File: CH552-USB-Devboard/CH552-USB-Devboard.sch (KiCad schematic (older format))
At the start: 38 parts, among them J1 Conn_01x11_Male, J2 Conn_01x11_Male, J3 USB_C_Receptacle, J4 USB_C_Receptacle, SW1 SW_Push, SW2 SW_Push, U1 CH552T, U2 CH552G

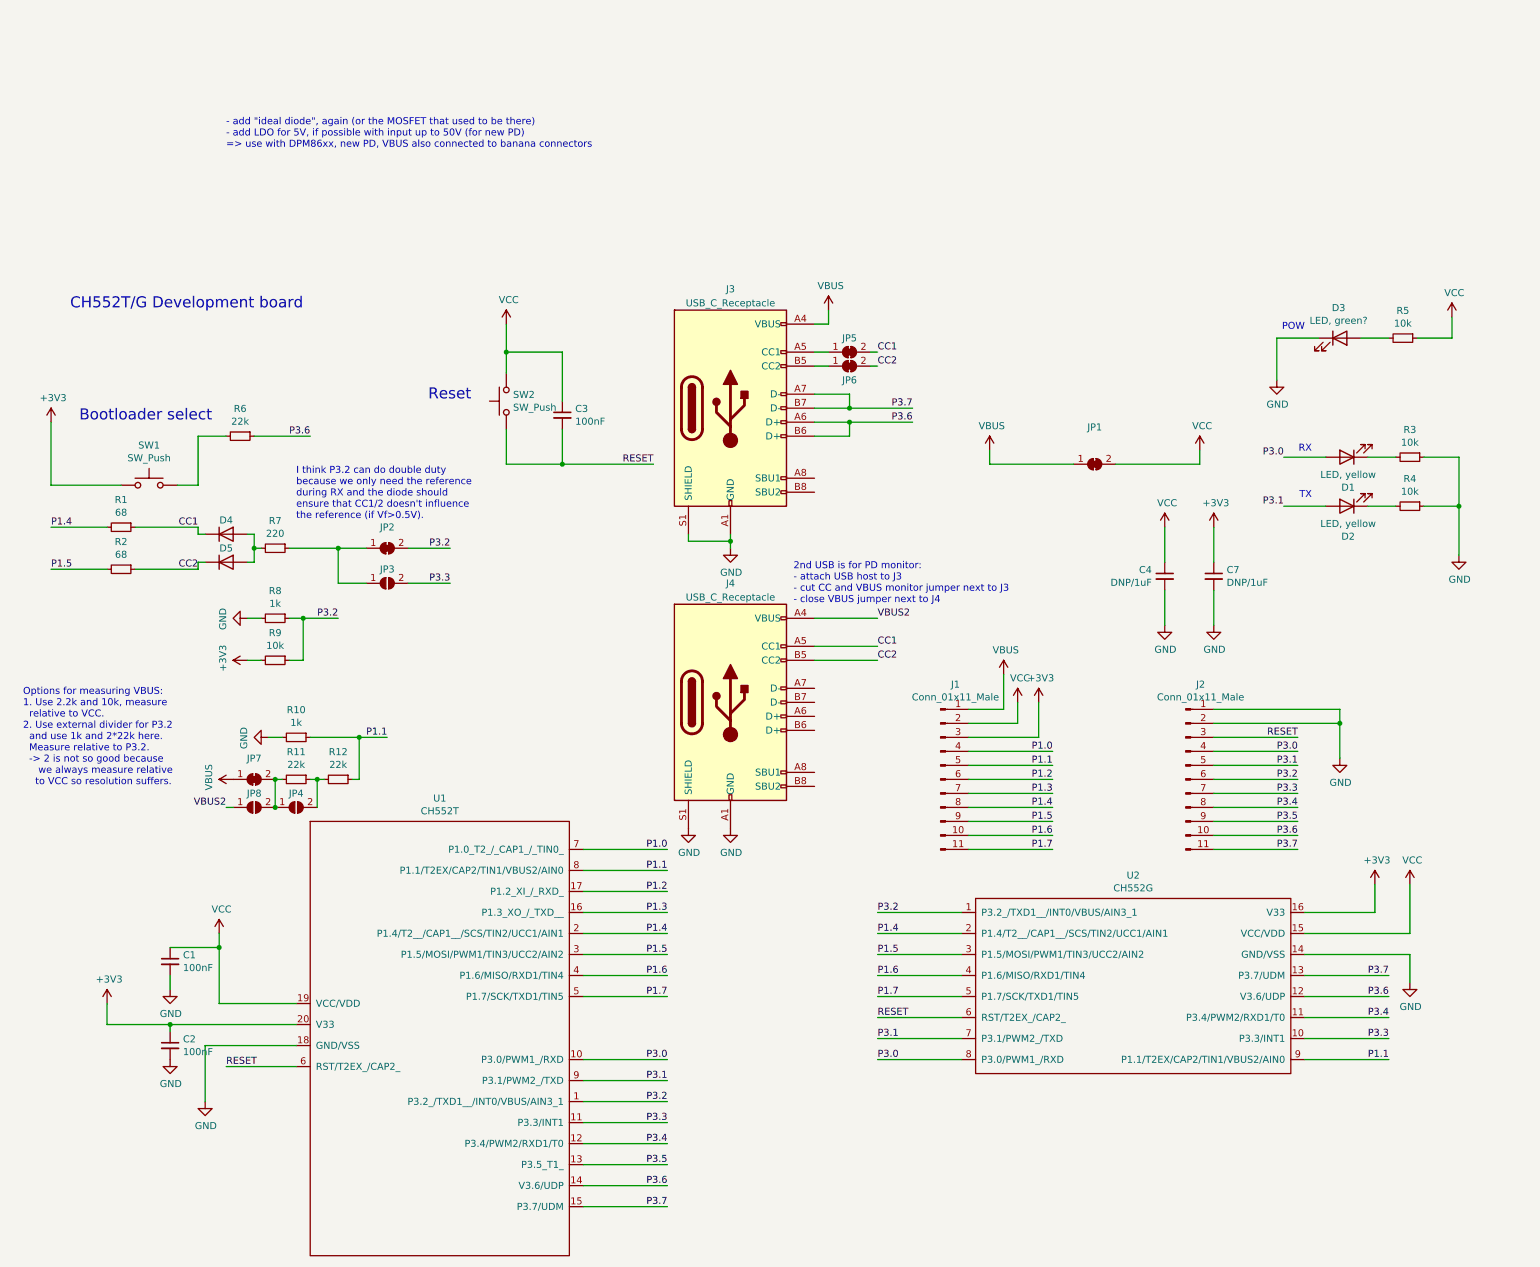
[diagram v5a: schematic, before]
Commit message: clean up schematic
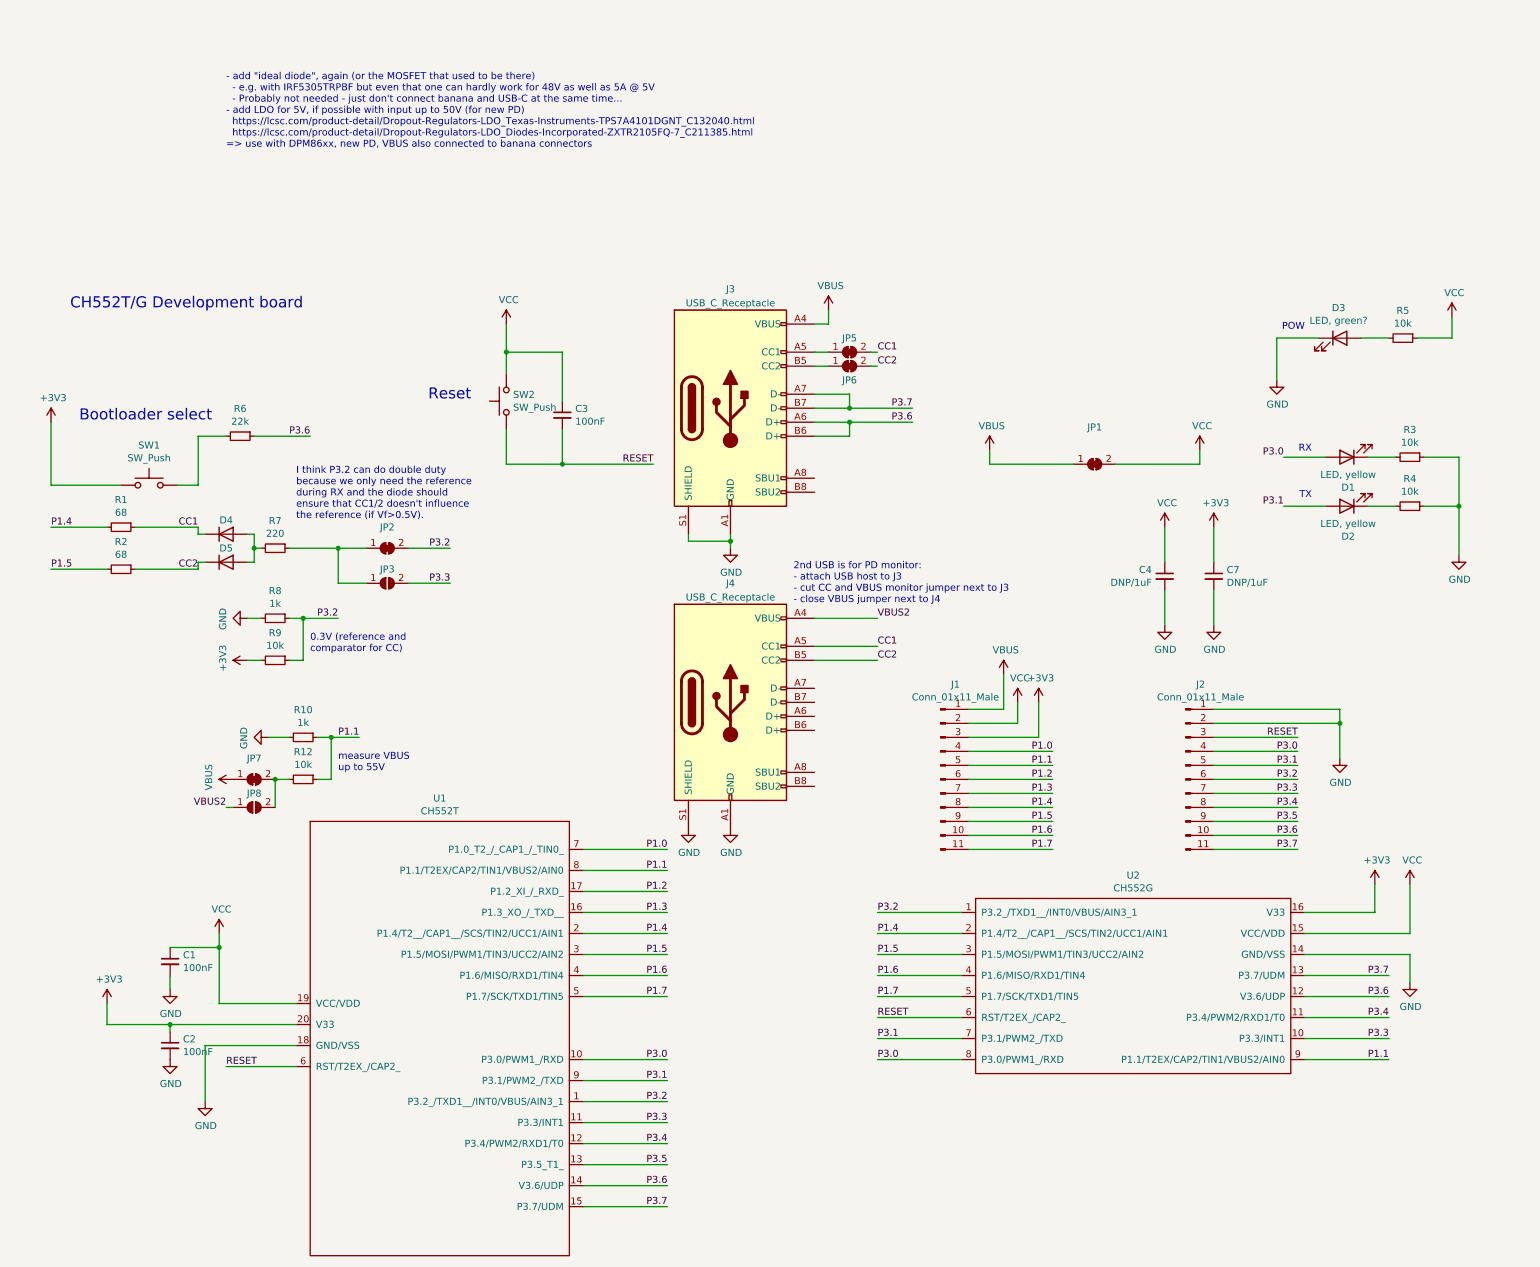
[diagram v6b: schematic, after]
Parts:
- removed JP4: Jumper, Jumper:SolderJumper-2_P1.3mm_Open_RoundedPad1.0x1.5mm, symbol Jumper:SolderJumper_2_Open
- removed R11: 22k, Resistor_SMD:R_0603_1608Metric_Pad0.98x0.95mm_HandSolder, symbol Device:R_Small
- J3, J4: DNP (none) -> PCBA; LCSC C283540 -> C165948
- R12: value 22k -> 10k; LCSC C31850 -> C25804
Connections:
- net at R12.2: now also JP7.2 (B), JP8.2 (B)
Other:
- note added: "- add "ideal diode", again (or the MOSFET that used to be there)\n - e.g. with IRF5305TRPBF but even that one can hardly work for 48V as well as 5A @ 5V\n - Probably not needed - just don't connect banana and USB-C at the same time...\n- add LDO for 5V, if possible with input up to 50V (for new PD)\n https://lcsc.com/product-detail/Dropout-Regulators-LDO_Texas-Instruments-TPS7A4101DGNT_C132040.ht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"
- note added: "0.3V (reference and\ncomparator for CC)"
- note added: "measure VBUS\nup to 55V"
- note removed: "- add "ideal diode", again (or the MOSFET that used to be there)\n- add LDO for 5V, if possible with input up to 50V (for new PD)\n=> use with DPM86xx, new PD, VBUS also connected to banana connectors"
- note removed: "Options for measuring VBUS:\n1. Use 2.2k and 10k, measure\n relative to VCC.\n2. Use external divider for P3.2\n and use 1k and 2*22k here.\n Measure relative to P3.2.\n -> 2 is not so good because\n we always measure relative\n to VCC so resolution suffers."
- moved on the sheet: R10, R12
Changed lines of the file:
@@
 F 2 "footprint:VACON_CSP_USC16_TR" H 5800 1450 50  0001 C CNN
 F 3 "http://www.usb.org/developers/docs/usb_31_033017.zip" H 5800 1450 50  0001 C CNN
-F 4 "C283540" H 5650 1450 50  0001 C CNN "LCSC"
+F 4 "C165948" H 5650 1450 50  0001 C CNN "LCSC"
+F 5 "PCBA" H 5650 1450 50  0001 C CNN "DNP"
 	1    5650 1450
 	1    0    0    -1
@@
 	6350 750  6350 850
 Wire Wire Line
-	3000 3800 3200 3800
-Text Label 3200 3800 2    50   ~ 0
+	2800 3800 3000 3800
+Text Label 3000 3800 2    50   ~ 0
 P1.1
 $Comp
 L Device:R_Small R10
 U 1 1 60B6EE8A
-P 2550 3800
-F 0 "R10" V 2354 3800 50  0000 C CNN
-F 1 "1k" V 2445 3800 50  0000 C CNN
-F 2 "Resistor_SMD:R_0603_1608Metric_Pad0.98x0.95mm_HandSolder" H 2550 3800 50  0001 C CNN
-F 3 "~" H 2550 3800 50  0001 C CNN
-F 4 "C21190" V 2550 3800 50  0001 C CNN "LCSC"
-	1    2550 3800
-	0    1    1    0
-$EndComp
-$Comp
-L Device:R_Small R11
-U 1 1 60B79ACF
-P 2550 4100
-F 0 "R11" V 2354 4100 50  0000 C CNN
-F 1 "22k" V 2445 4100 50  0000 C CNN
-F 2 "Resistor_SMD:R_0603_1608Metric_Pad0.98x0.95mm_HandSolder" H 2550 4100 50  0001 C CNN
-F 3 "~" H 2550 4100 50  0001 C CNN
-F 4 "C31850" V 2550 4100 50  0001 C CNN "LCSC"
-	1    2550 4100
+P 2600 3800
+F 0 "R10" V 2404 3800 50  0000 C CNN
+F 1 "1k" V 2495 3800 50  0000 C CNN
+F 2 "Resistor_SMD:R_0603_1608Metric_Pad0.98x0.95mm_HandSolder" H 2600 3800 50  0001 C CNN
+F 3 "~" H 2600 3800 50  0001 C CNN
+F 4 "C21190" V 2600 3800 50  0001 C CNN "LCSC"
+	1    2600 3800
 	0    1    1    0
 $EndComp
@@
 $EndComp
 Wire Wire Line
-	2450 3800 2350 3800
+	2500 3800 2350 3800
 Wire Wire Line
-	3000 4100 3000 3800
-Connection ~ 3000 3800
-Text Notes 600  4150 0    50   ~ 0
-Options for measuring VBUS:\n1. Use 2.2k and 10k, measure\n  relative to VCC.\n2. Use external divider for P3.2\n  and use 1k and 2*22k here.\n  Measure relative to P3.2.\n  -> 2 is not so good because\n     we always measure relative\n    to VCC so resolution suffers.
+	2800 4100 2800 3800
+Connection ~ 2800 3800
+Text Notes 2850 4050 0    50   ~ 0
+measure VBUS\nup to 55V
 $Comp
 L Device:R_Small R12
 U 1 1 60BB508E
-P 2850 4100
-F 0 "R12" V 2654 4100 50  0000 C CNN
-F 1 "22k" V 2745 4100 50  0000 C CNN
-F 2 "Resistor_SMD:R_0603_1608Metric_Pad0.98x0.95mm_HandSolder" H 2850 4100 50  0001 C CNN
-F 3 "~" H 2850 4100 50  0001 C CNN
-F 4 "C31850" V 2850 4100 50  0001 C CNN "LCSC"
-	1    2850 4100
+P 2600 4100
+F 0 "R12" V 2404 4100 50  0000 C CNN
+F 1 "10k" V 2495 4100 50  0000 C CNN
+F 2 "Resistor_SMD:R_0603_1608Metric_Pad0.98x0.95mm_HandSolder" H 2600 4100 50  0001 C CNN
+F 3 "~" H 2600 4100 50  0001 C CNN
+F 4 "C25804" V 2600 4100 50  0001 C CNN "LCSC"
+	1    2600 4100
 	0    1    1    0
 $EndComp
 Wire Wire Line
-	2650 3800 3000 3800
-$Comp
-L Jumper:SolderJumper_2_Open JP4
-U 1 1 60BC9416
-P 2550 4300
-F 0 "JP4" H 2550 4400 50  0000 C CNN
-F 1 "Jumper" H 2550 4473 50  0001 C CNN
-F 2 "Jumper:SolderJumper-2_P1.3mm_Open_RoundedPad1.0x1.5mm" H 2550 4300 50  0001 C CNN
-F 3 "~" H 2550 4300 50  0001 C CNN
-	1    2550 4300
-	1    0    0    -1
-$EndComp
+	2700 3800 2800 3800
 Wire Wire Line
-	2950 4100 3000 4100
-Wire Wire Line
-	2700 4300 2700 4100
-Wire Wire Line
-	2700 4100 2650 4100
-Wire Wire Line
-	2700 4100 2750 4100
-Connection ~ 2700 4100
-Wire Wire Line
-	2400 4100 2450 4100
+	2700 4100 2800 4100
 $Comp
 L Connector:USB_C_Receptacle_USB2.0 J4
@@
 F 2 "footprint:VACON_CSP_USC16_TR" H 5800 3550 50  0001 C CNN
 F 3 "http://www.usb.org/developers/docs/usb_31_033017.zip" H 5800 3550 50  0001 C CNN
-F 4 "C283540" H 5650 3550 50  0001 C CNN "LCSC"
+F 4 "C165948" H 5650 3550 50  0001 C CNN "LCSC"
+F 5 "PCBA" H 5650 3550 50  0001 C CNN "DNP"
 	1    5650 3550
 	1    0    0    -1
@@
 Wire Wire Line
 	2400 4300 2400 4100
-Connection ~ 2400 4300
 Connection ~ 2400 4100
 Text Notes 2050 -400 0    50   ~ 0
-- add "ideal diode", again (or the MOSFET that used to be there)\n- add LDO for 5V, if possible with input up to 50V (for new PD)\n=> use with DPM86xx, new PD, VBUS also connected to banana connectors
+- add "ideal diode", again (or the MOSFET that used to be there)\n  - e.g. with IRF5305TRPBF but even that one can hardly work for 48V as well as 5A @ 5V\n  - Probably not needed - just don't connect banana and USB-C at the same time...\n- add LDO for 5V, if possible with input up to 50V (for new PD)\n  https://lcsc.com/product-detail/Dropout-Regulators-LDO_Texas-Instruments-TPS7A4101DGNT_C132040.html\n  https://lcsc.com/product-detail/Dropout-Regulators-LDO_Diodes-Incorporated-ZXTR2105FQ-7_C211385.html\n=> use with DPM86xx, new PD, VBUS also connected to banana connectors
+Text Notes 2650 3200 0    50   ~ 0
+0.3V (reference and\ncomparator for CC)
+Wire Wire Line
+	2400 4100 2500 4100
 $EndSCHEMATC

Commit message: stop using the rescue library
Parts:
- U1: symbol CH552-USB-Devboard-rescue:CH552T-MCU_WCH -> CH552-USB-Devboard:CH552T-MCU_WCH
- U2: symbol CH552-USB-Devboard-rescue:CH552G-MCU_WCH -> CH552-USB-Devboard:CH552G-MCU_WCH
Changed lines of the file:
@@
 $EndComp
 $Comp
-L CH552-USB-Devboard-rescue:CH552T-MCU_WCH U1
+L CH552-USB-Devboard:CH552T-MCU_WCH U1
 U 1 1 5E91FA86
 P 3800 5200
@@
 $EndComp
 $Comp
-L CH552-USB-Devboard-rescue:CH552G-MCU_WCH U2
+L CH552-USB-Devboard:CH552G-MCU_WCH U2
 U 1 1 5E91FB0A
 P 8550 5500

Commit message: add LDO for VCC (5V)
It supports VBUS up to 48V because that's what future USB PD will
use and we want to support that.
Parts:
- added C? (x2): 4u7, 50V, Capacitor_SMD:C_1206_3216Metric_Pad1.33x1.80mm_HandSolder, symbol Device:C_Small
- added C?: 10uF, Capacitor_SMD:C_0603_1608Metric_Pad1.05x0.95mm_HandSolder, symbol Device:C_Small
- added C?: 100nF, Capacitor_SMD:C_0603_1608Metric_Pad1.05x0.95mm_HandSolder, symbol Device:C_Small
- added C?: 10nF, Capacitor_SMD:C_0603_1608Metric_Pad1.05x0.95mm_HandSolder, symbol Device:C_Small
- added R?: 62k, Resistor_SMD:R_0603_1608Metric_Pad0.98x0.95mm_HandSolder, symbol Device:R_Small
- added R?: 22k, Resistor_SMD:R_0603_1608Metric_Pad0.98x0.95mm_HandSolder, symbol Device:R_Small
- added R?: DNP / 68k, Resistor_SMD:R_0603_1608Metric_Pad0.98x0.95mm_HandSolder, symbol Device:R_Small
- added U?: TPS7A4101DGNT, CH552-USB-Devboard:HVSSOP-8_3.0x3.0mm_P0.65mm, symbol CH552-USB-Devboard:TPS7A4101DGNT
- JP1: footprint Jumper:SolderJumper-2_P1.3mm_Bridged_RoundedPad1.0x1.5mm -> Jumper:SolderJumper-2_P1.3mm_Open_RoundedPad1.0x1.5mm; symbol Jumper:SolderJumper_2_Bridged -> Jumper:SolderJumper_2_Open
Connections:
- net GND: now also C?.2, C?.2, C?.2, R?.1, U?.4 (GND), U?.EP (GND)
- net VBUS: now also C?.1, U?.8 (IN), U?.EN (5)
- net VCC: now also C?.1, C?.1, C?.1, R?.2, R?.2, U?.1 (OUT)
- new net: C?.2, R?.1, R?.1, R?.2, U?.2 (FB)
- new net: C?.1, C?.2
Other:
- note added: "0.3V (Vref and\ncomparator for CC)"
- note added: "11 mA for MCU plus CC\ncurrent (17 mA but not\ncontinuous)"
- note added: "CC RX: ACMP P1.4/5 to 0.3V on P3.2\nCC TX 0: drive 0 on P1.4/5\nCC TX 1: drive P1.4/5 to GND\n and P3.2 to high"
- note added: "Vref=1.173\n(Vout=4.8V with 68k)\nVout=4.5V with 62k\nIout=23mA -> 1W,\n -> 70°C over ambient"
- note removed: "0.3V (reference and\ncomparator for CC)"
- moved on the sheet: D3, R5
